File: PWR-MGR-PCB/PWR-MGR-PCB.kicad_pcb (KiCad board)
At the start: 2 copper layers, 30 x 35 mm, 30 parts, among them J1 Conn_01x02_Pin, J3 USB_C_Receptacle_USB2.0_14P, J4 Battery_1x2, J5 Conn_01x02_Pin, U2 BQ24074RGT, U5 USBLC6-2SC6, U6 TPS631011YBGR

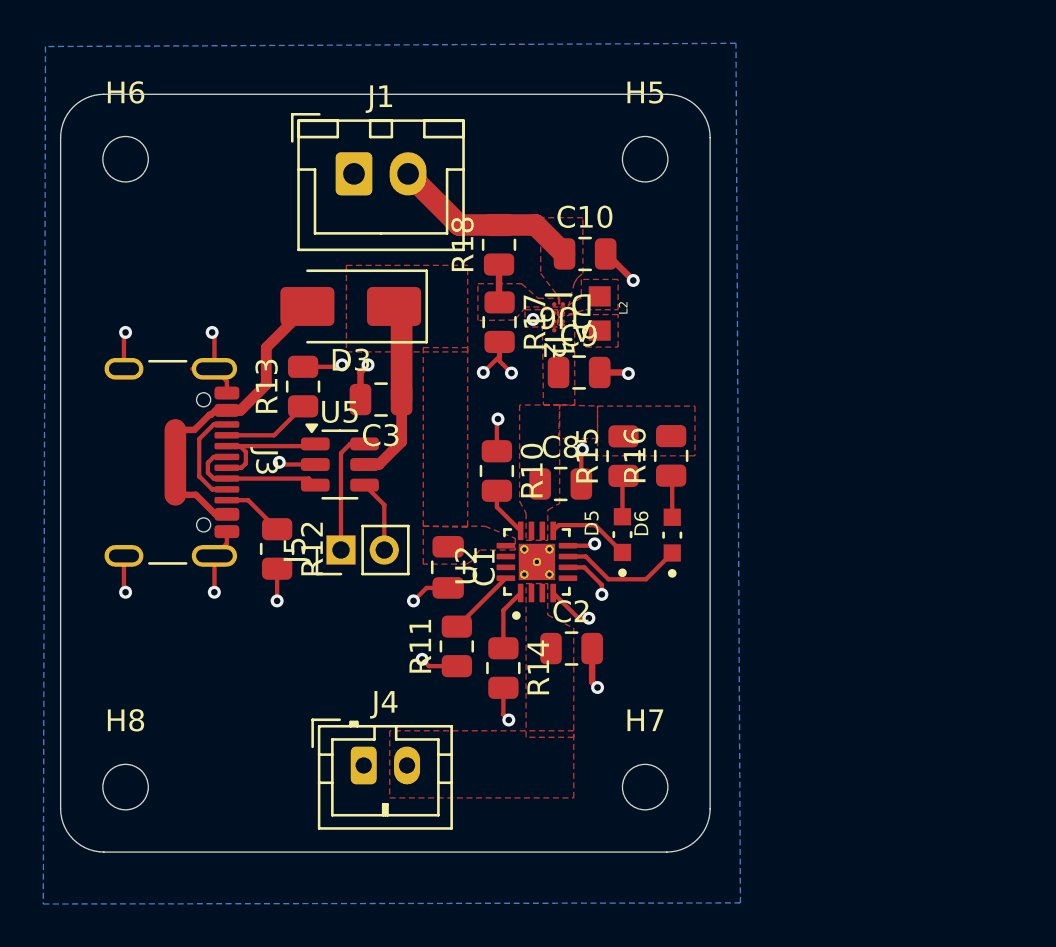
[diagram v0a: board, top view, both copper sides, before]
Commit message: Add BQ24075
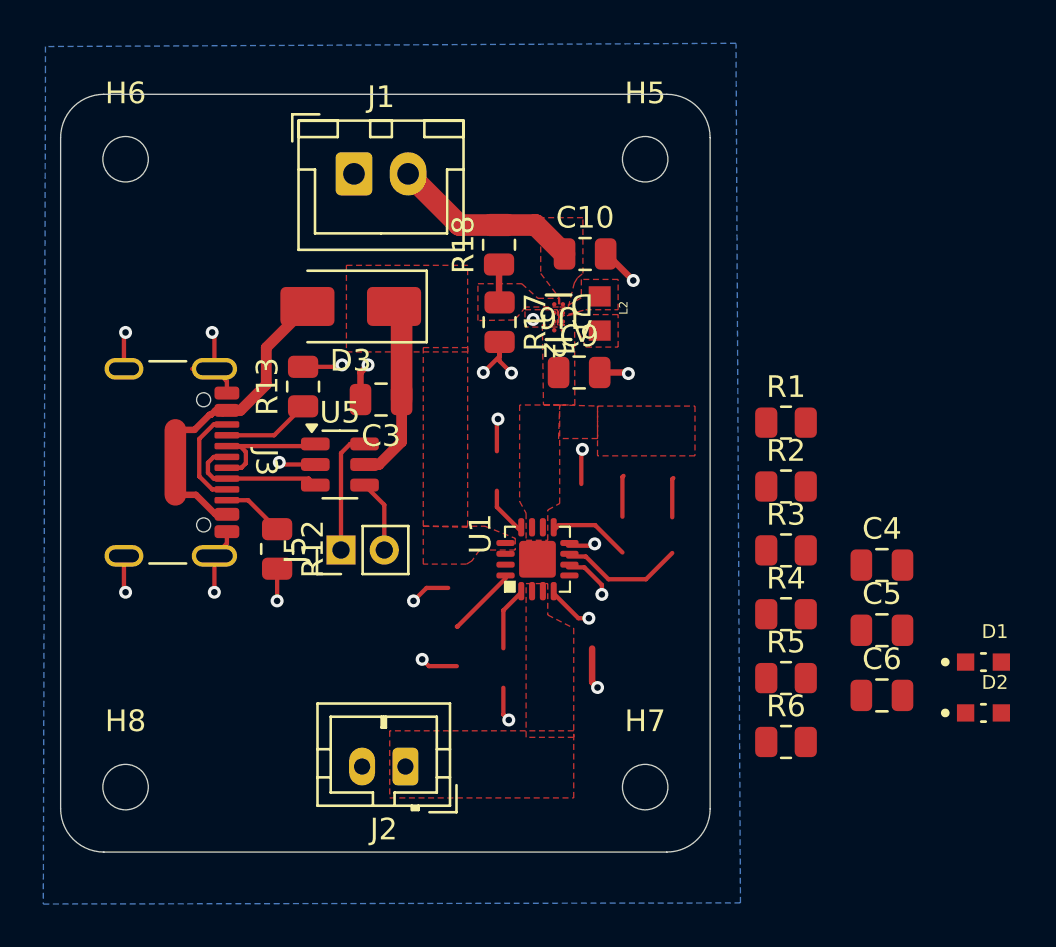
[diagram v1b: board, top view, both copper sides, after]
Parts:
- removed C1: 1uF, Capacitor_SMD:C_0805_2012Metric
- removed C2, C8: 4.7uF, Capacitor_SMD:C_0805_2012Metric
- removed D5, D6: SML-D12U1WT86, LED - SML_D12U1WT86:LED_SML-D12U1WT86
- removed J4: Battery_1x2, Connector_JST:JST_PH_B2B-PH-K_1x02_P2.00mm_Vertical
- removed R10: 1.18k, Resistor_SMD:R_0805_2012Metric
- removed R11: 1.13k, Resistor_SMD:R_0805_2012Metric
- removed R14: 10k, Resistor_SMD:R_0805_2012Metric
- removed R15, R16: 1k, Resistor_SMD:R_0805_2012Metric
- removed U2: BQ24074RGT, BQ24074RGTR:QFN50P300X300X100-17N
- added C4: 4.7uF, Capacitor_SMD:C_0805_2012Metric, F.Cu at (177.9, 101.7)
- added C5: 1uF, Capacitor_SMD:C_0805_2012Metric, F.Cu at (177.9, 104.8)
- added C6: 4.7uF, Capacitor_SMD:C_0805_2012Metric, F.Cu at (177.9, 107.8)
- added D1: SML-D12U1WT86, LED - SML_D12U1WT86:LED_SML-D12U1WT86, F.Cu at (182.6, 106.2)
- added D2: SML-D12U1WT86, LED - SML_D12U1WT86:LED_SML-D12U1WT86, F.Cu at (182.6, 108.6)
- added J2: Battery_1x2, Connector_JST:JST_PH_B2B-PH-K_1x02_P2.00mm_Vertical, F.Cu at (155.9, 111.0)
- added R1: 1.18k, Resistor_SMD:R_0805_2012Metric, F.Cu at (173.5, 95.2)
- added R2: 1.13k, Resistor_SMD:R_0805_2012Metric, F.Cu at (173.5, 98.1)
- added R3: 46.4k, Resistor_SMD:R_0805_2012Metric, F.Cu at (173.5, 101.1)
- added R4: 10k, Resistor_SMD:R_0805_2012Metric, F.Cu at (173.5, 104.0)
- added R5: 1k, Resistor_SMD:R_0805_2012Metric, F.Cu at (173.5, 107.0)
- added R6: 1k, Resistor_SMD:R_0805_2012Metric, F.Cu at (173.5, 109.9)
- added U1: BQ24075, BQ24075:QFN16, F.Cu at (162.0, 101.5)
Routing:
- net Net-(U2-~{PGOOD}): track 5.75 -> 0.00 mm
- net Net-(U1-PGOOD): track 0.00 -> 5.75 mm
- net Net-(U2-~{CHG}): track 3.83 -> 0.00 mm
- net Net-(U1-CHG): track 0.00 -> 3.83 mm
- net (no net): track 4.81 -> 8.55 mm
- net Net-(U2-ISET): track 3.19 -> 0.00 mm
- net Net-(U1-ISET): track 0.00 -> 3.19 mm
- net Net-(U2-TS): track 2.88 -> 0.00 mm
- net Net-(U1-TS): track 0.00 -> 2.88 mm
- net Net-(U2-ILIM): track 2.31 -> 0.00 mm
- net Net-(U1-ILIM): track 0.00 -> 2.31 mm
- net Net-(D5-PadA): track 1.91 -> 0.00 mm
- net Net-(D6-PadA): track 1.83 -> 0.00 mm
- added copper zone on F.Cu, net (none)
- removed copper zone on F.Cu, net /PWR-MGR-01/V_BATT

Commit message: Route BQ24075
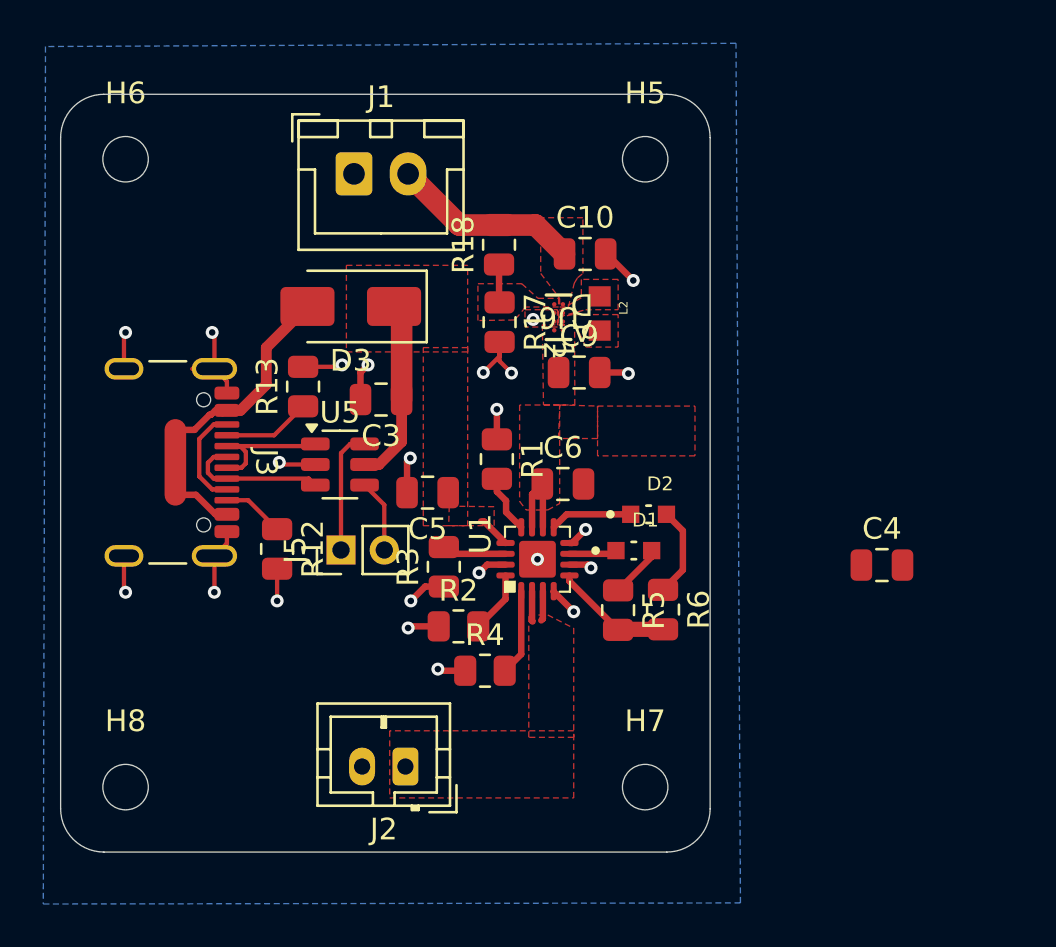
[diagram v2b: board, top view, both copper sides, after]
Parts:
- R5, R6: value 1k -> 1.5k
- moved C5 21.9 mm to (156.9, 98.4), turned to 180 degrees
- moved D2 18.0 mm to (167.2, 99.4)
- moved C6 17.7 mm to (163.2, 98.0)
- moved D1 17.0 mm to (166.5, 101.1)
- moved R2 16.5 mm to (158.4, 104.6)
- moved R3 15.8 mm to (157.7, 101.8), turned to 90 degrees
- moved R4 14.1 mm to (159.6, 106.6)
- moved R1 13.5 mm to (160.2, 96.8), turned to -90 degrees
- moved R5 8.37 mm to (165.8, 103.8), turned to -90 degrees
- moved R6 8.35 mm to (167.8, 103.8), turned to -90 degrees
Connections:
- net Net-(J2-Pin_1) renamed /PWR-MGR-01/BATT+
- U1 pad 11: unconnected-(U1-OUT-Pad11) -> VCC_BMS
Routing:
- net VCC_BMS: track 0.00 -> 9.74 mm
- net Net-(D2-PadA): track 0.00 -> 4.18 mm
- net (no net): track 8.55 -> 4.81 mm
- net GND: track 40.7 -> 37.2 mm, vias 22 -> 23
- net Net-(U1-PGOOD): track 5.75 -> 2.21 mm
- net Net-(U1-TMR): track 0.00 -> 2.98 mm
- net /PWR-MGR-01/BATT+: track 0.00 -> 2.79 mm
- net Net-(D1-PadA): track 0.00 -> 2.48 mm
- net VBUS 5V: track 8.90 -> 10.4 mm
- net Net-(U1-TS): track 2.88 -> 3.99 mm
- added copper zone on F.Cu, net /PWR-MGR-01/BATT+
- removed copper zone on F.Cu, net (none)

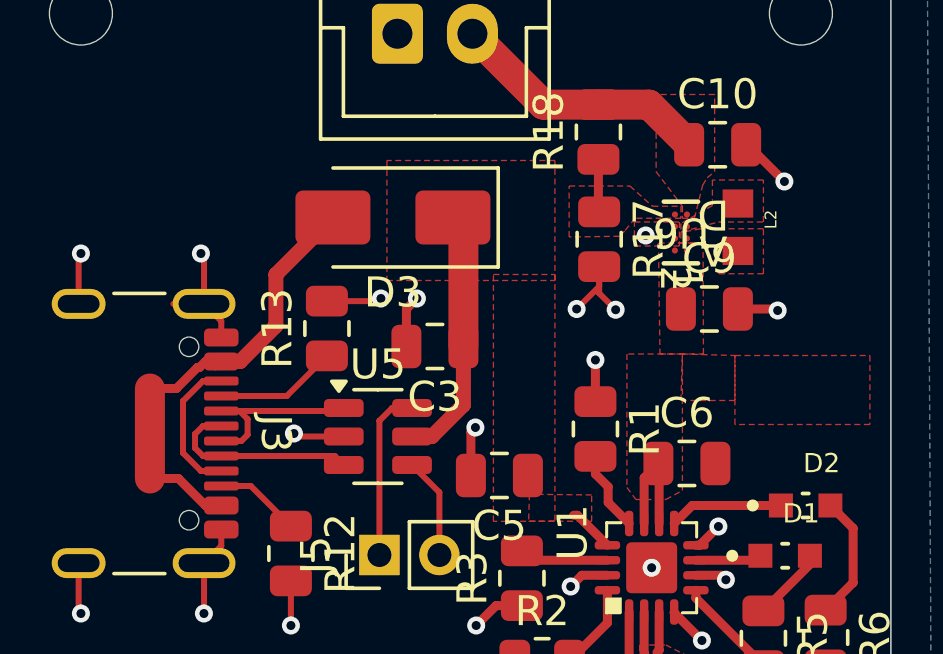
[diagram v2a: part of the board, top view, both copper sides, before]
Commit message: Fix SBU tracks
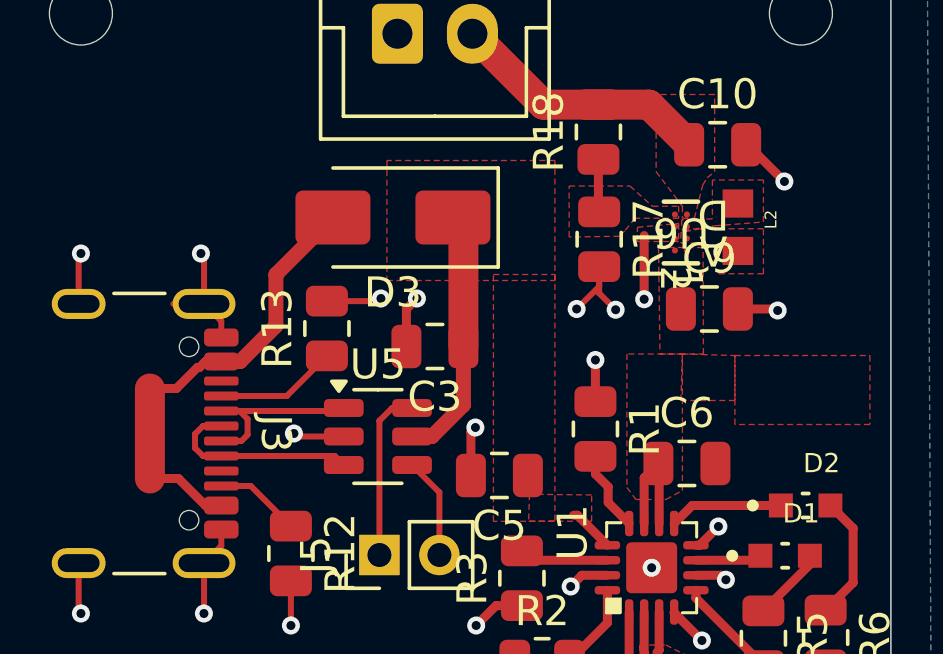
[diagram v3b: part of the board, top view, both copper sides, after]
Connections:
- U1 pad 11: VCC_BMS -> unconnected-(U1-OUT-Pad11)
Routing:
- net (no net): track 4.81 -> 0.00 mm
- net GND: track 37.2 -> 39.3 mm
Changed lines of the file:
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@@
 	(net 22 "Net-(U6-LX1)")
 	(net 23 "Net-(U1-TS)")
+	(net 24 "unconnected-(U1-OUT-Pad11)")
 	(footprint "Capacitor_SMD:C_0805_2012Metric"
 		(layer "F.Cu")
@@
 			(layers "F.Cu")
 			(roundrect_rratio 0.375)
-			(net 1 "VCC_BMS")
+			(net 24 "unconnected-(U1-OUT-Pad11)")
 			(pinfunction "OUT")
 			(pintype "bidirectional")
@@
 	)
 	(segment
-		(start 146.403 97.648924)
-		(end 147.004076 98.25)
-		(width 0.2)
-		(layer "F.Cu")
-		(net 0)
-	)
-	(segment
-		(start 146.403 95.918176)
-		(end 146.403 97.648924)
-		(width 0.2)
-		(layer "F.Cu")
-		(net 0)
-	)
-	(segment
-		(start 147.68 95.25)
-		(end 147.071176 95.25)
-		(width 0.2)
-		(layer "F.Cu")
-		(net 0)
-	)
-	(segment
-		(start 147.071176 95.25)
-		(end 146.403 95.918176)
-		(width 0.2)
-		(layer "F.Cu")
-		(net 0)
-	)
-	(segment
-		(start 147.004076 98.25)
-		(end 147.68 98.25)
-		(width 0.2)
-		(layer "F.Cu")
-		(net 0)
-	)
-	(segment
 		(start 163.5 102.4875)
 		(end 165.75 104.7375)
@@
 	)
 	(segment
+		(start 161.775 92.525)
+		(end 161.775 90.4)
+		(width 0.3)
+		(layer "F.Cu")
+		(net 2)
+	)
+	(segment
 		(start 157.5 106.625)
 		(end 157.425 106.55)
@@
 	)
 	(via
-		(at 161.825 90.4)
+		(at 161.775 92.525)
 		(size 0.6)
 		(drill 0.3)
 		(layers "F.Cu" "B.Cu")
-		(free yes)
 		(net 2)
 	)
@@
 		(polygon
 			(pts
-				(xy 162.95 89.95) (xy 162.95 90.75) (xy 161.45 90.75) (xy 161.45 89.95)
+				(xy 162.925 90) (xy 162.925 90.6) (xy 161.55 90.6) (xy 161.55 90.125)
 			)
 		)
@@
 		(polygon
 			(pts
-				(xy 163 90.270828) (xy 163.022975 90.277207) (xy 164.25 89.95) (xy 165.75 89.95) (xy 165.75 88.55)
-				(xy 164.05 88.55) (xy 164.05 89.4) (xy 163 90)
+				(xy 163.025 90.175) (xy 163.085348 90.235348) (xy 164.15 90.075) (xy 165.75 89.95) (xy 165.75 88.55)
+				(xy 164.05 88.55) (xy 164.05 89.846419) (xy 163.025 89.875)
 			)
 		)
@@
 		(polygon
 			(pts
-				(xy 163.740123 90.65) (xy 162.25137 90.65) (xy 162.302055 94.35) (xy 163.75 94.35)
+				(xy 163.740523 90.8) (xy 162.253425 90.8) (xy 162.302055 94.35) (xy 163.75 94.35)
 			)
 		)
@@
 		(polygon
 			(pts
-				(xy 163 89.425) (xy 163 89.825) (xy 161.475 89.825) (xy 161.125 90.25) (xy 160.95 90.425) (xy 159.275 90.45)
-				(xy 159.275 88.75) (xy 161.3 88.75) (xy 162.05 89.425)
+				(xy 162.925 89.425) (xy 162.925 89.825) (xy 161.475 89.825) (xy 161.125 90.25) (xy 160.95 90.425)
+				(xy 159.275 90.45) (xy 159.275 88.75) (xy 161.3 88.75) (xy 162.05 89.425)
 			)
 		)

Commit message: Solve all DRC issues
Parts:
- moved C4 15.3 mm to (163.5, 106.7)
- moved R6 4.66 mm to (167.1, 99.2), turned to 180 degrees
- moved D1 3.58 mm to (167.2, 104.6)
- moved R5 1.75 mm to (167.2, 102.8), turned to 180 degrees
- moved D2 1.55 mm to (167.1, 101.0)
- moved J2 1.13 mm to (156.3, 112.1)
- moved C6 0.46 mm to (163.3, 97.6)
- moved J1 0.17 mm to (153.4, 83.5)
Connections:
- U1 pad 11: unconnected-(U1-OUT-Pad11) -> VCC_BMS
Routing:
- net VCC_BMS: track 9.74 -> 20.8 mm
- net GND: track 39.3 -> 44.0 mm, vias 23 -> 24
- net Net-(U1-PGOOD): track 2.21 -> 5.08 mm
- net Net-(U6-FB): track 1.76 -> 4.25 mm
- net Net-(D2-PadA): track 4.18 -> 1.76 mm
- net +3.3V: track 8.76 -> 11.0 mm
- net Net-(D1-PadA): track 2.48 -> 1.77 mm
- removed copper zone on F.Cu, net +3.3V
- removed copper zone on F.Cu, net Net-(U6-FB)

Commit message: Solve all ERC issues
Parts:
- U6: value TPS631011YBGR -> TPS631011YBGR-Pin_Corrected
- moved J3 0.28 mm to (143.7, 97.1)
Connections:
- U1 pad 11: VCC_BMS -> unconnected-(U1-OUT-Pad11)
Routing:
- net GND: track 44.0 -> 41.7 mm
- net VCC_BMS: track 20.8 -> 19.3 mm
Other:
- board text added: "+"
- board text added: "-"
- board text added: "- +"
- board text added: "PWR-MGR-PCB V1"

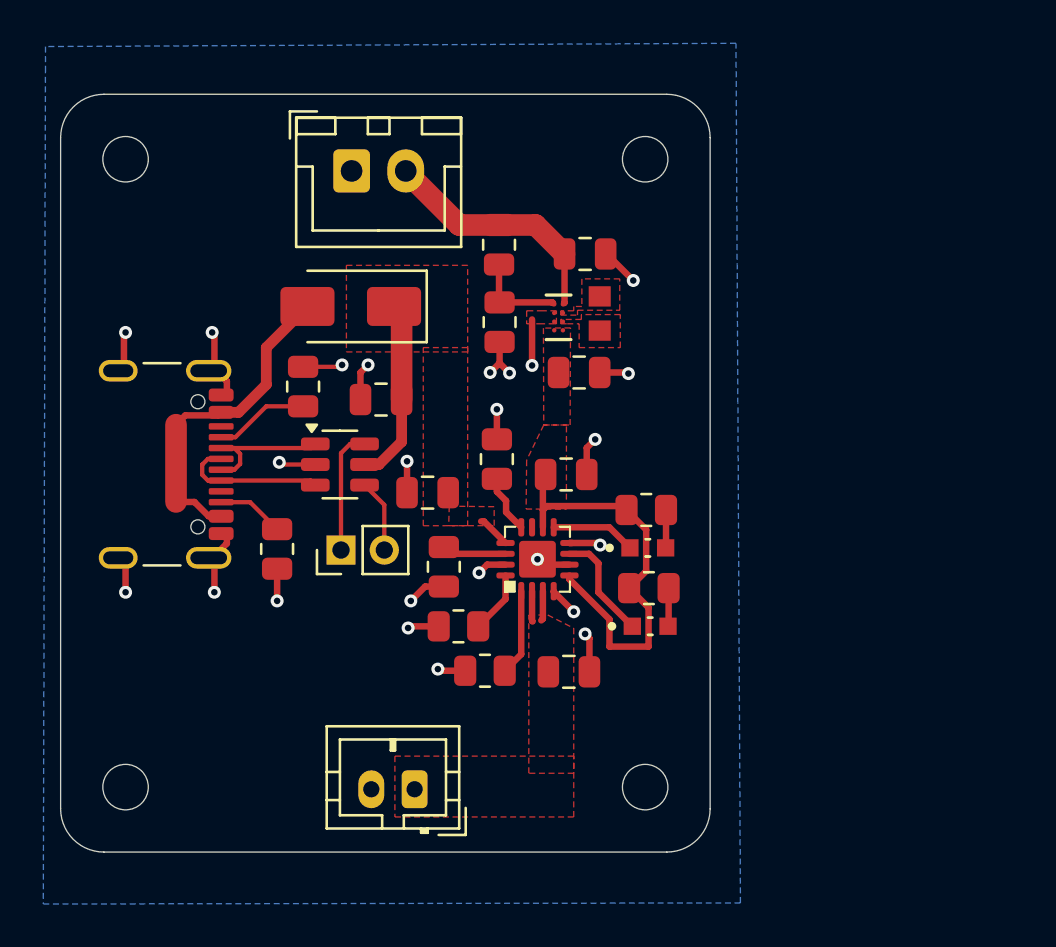
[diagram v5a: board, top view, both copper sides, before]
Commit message: Add MPNs and generate DRL file
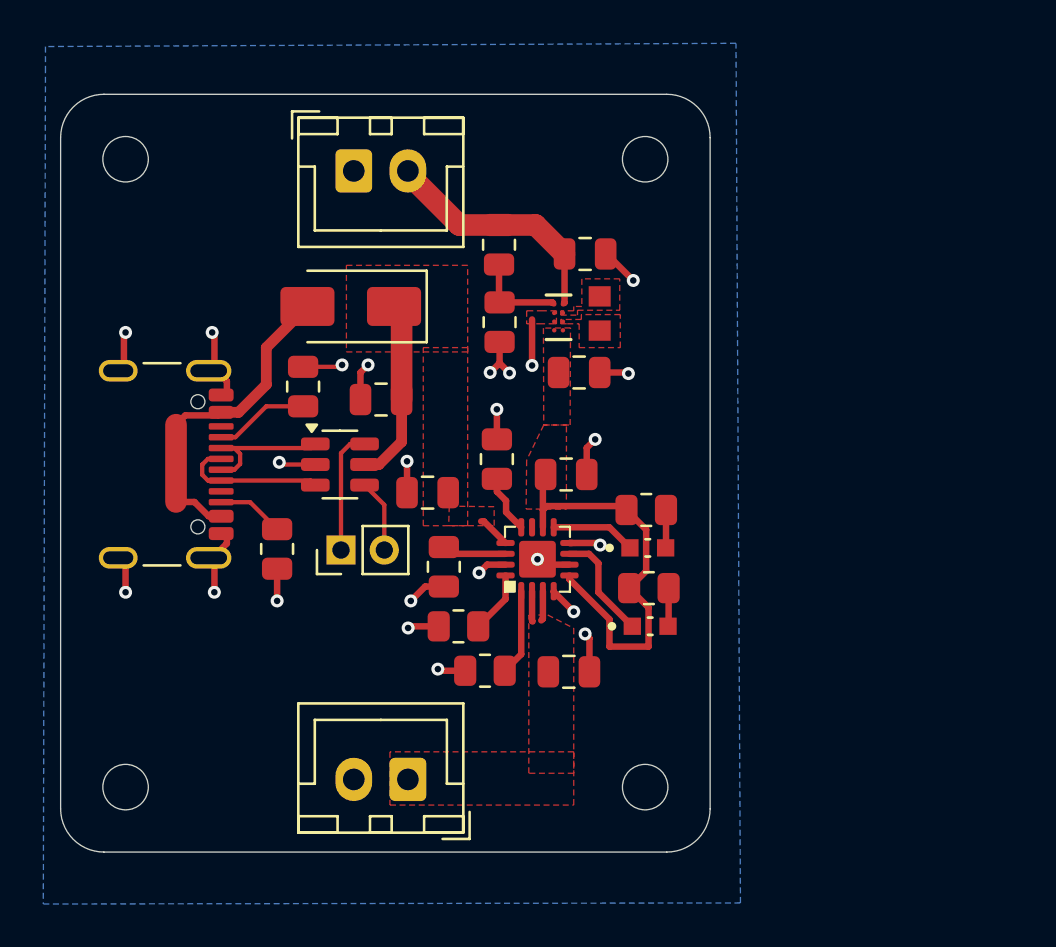
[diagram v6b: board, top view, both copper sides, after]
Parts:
- J2: footprint Connector_JST:JST_PH_B2B-PH-K_1x02_P2.00mm_Vertical -> Connector_JST:JST_XH_B2B-XH-A_1x02_P2.50mm_Vertical
- moved J2 0.55 mm to (156.0, 111.6)
- moved J1 0.10 mm to (153.5, 83.5)

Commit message: Adjust boost converter FB pin
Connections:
- U1 pad 11: unconnected-(U1-OUT-Pad11) -> VCC_BMS
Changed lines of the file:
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@@
 	(net 20 "Net-(U6-LX1)")
 	(net 21 "Net-(U1-TS)")
-	(net 22 "unconnected-(U1-OUT-Pad11)")
-	(net 23 "Net-(U1-PGOOD)")
-	(net 24 "Net-(U1-CHG)")
+	(net 22 "Net-(U1-PGOOD)")
+	(net 23 "Net-(U1-CHG)")
 	(footprint "Capacitor_SMD:C_0805_2012Metric"
 		(layer "F.Cu")
@@
 			(size 0.8 0.8)
 			(layers "F.Cu" "F.Mask" "F.Paste")
-			(net 23 "Net-(U1-PGOOD)")
+			(net 22 "Net-(U1-PGOOD)")
 			(pintype "passive")
 			(solder_mask_margin 0.102)
@@
 			)
 		)
-		(property "Manufacturer Part Number" ""
+		(property "Manufacturer Part Number" "USB4105-GF-A"
 			(at 0 0 270)
 			(unlocked yes)
@@
 			(size 0.8 0.8)
 			(layers "F.Cu" "F.Mask" "F.Paste")
-			(net 24 "Net-(U1-CHG)")
+			(net 23 "Net-(U1-CHG)")
 			(pintype "passive")
 			(solder_mask_margin 0.102)
@@
 			)
 		)
-		(property "Manufacturer Part Number" "  USBLC6-2SC6"
+		(property "Manufacturer Part Number" "USBLC6-2SC6"
 			(at 0 0 0)
 			(unlocked yes)
@@
 			)
 		)
-		(property "Manufacturer Part Number" ""
+		(property "Manufacturer Part Number" "TMM-102-02-T-S"
 			(at 0 0 90)
 			(unlocked yes)
@@
 			(layers "F.Cu")
 			(roundrect_rratio 0.375)
-			(net 23 "Net-(U1-PGOOD)")
+			(net 22 "Net-(U1-PGOOD)")
 			(pinfunction "PGOOD")
 			(pintype "bidirectional")
@@
 			(layers "F.Cu")
 			(roundrect_rratio 0.375)
-			(net 24 "Net-(U1-CHG)")
+			(net 23 "Net-(U1-CHG)")
 			(pinfunction "CHG")
 			(pintype "bidirectional")
@@
 			(layers "F.Cu")
 			(roundrect_rratio 0.375)
-			(net 22 "unconnected-(U1-OUT-Pad11)")
+			(net 1 "VCC_BMS")
 			(pinfunction "OUT")
-			(pintype "power_out+no_connect")
+			(pintype "power_out")
 		)
 		(pad "12" smd roundrect
@@
 		(width 0.3)
 		(layer "F.Cu")
-		(net 23)
+		(net 22)
 	)
 	(segment
@@
 		(width 0.3)
 		(layer "F.Cu")
-		(net 23)
+		(net 22)
 	)
 	(segment
@@
 		(width 0.3)
 		(layer "F.Cu")
-		(net 23)
+		(net 22)
 	)
 	(segment
@@
 		(width 0.3)
 		(layer "F.Cu")
-		(net 23)
+		(net 22)
 	)
 	(segment
@@
 		(width 0.3)
 		(layer "F.Cu")
-		(net 24)
+		(net 23)
 	)
 	(segment
@@
 		(width 0.3)
 		(layer "F.Cu")
-		(net 24)
+		(net 23)
 	)
 	(zone
